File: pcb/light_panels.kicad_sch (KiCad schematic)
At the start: 31 parts, among them Y1 32.768kHz

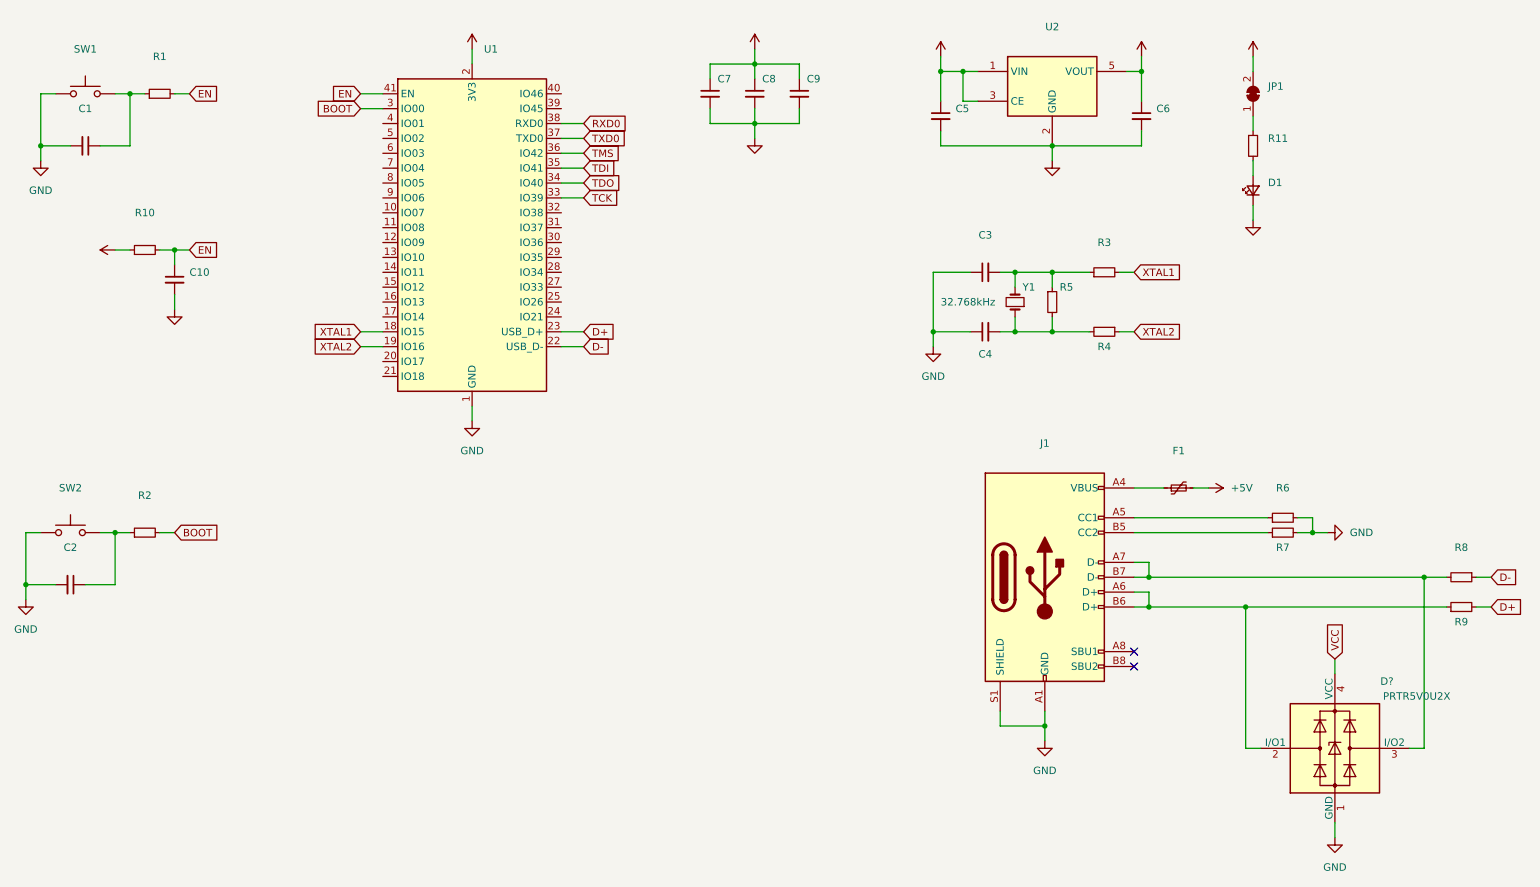
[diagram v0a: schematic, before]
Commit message: Added ferrite beads FB1 and 2
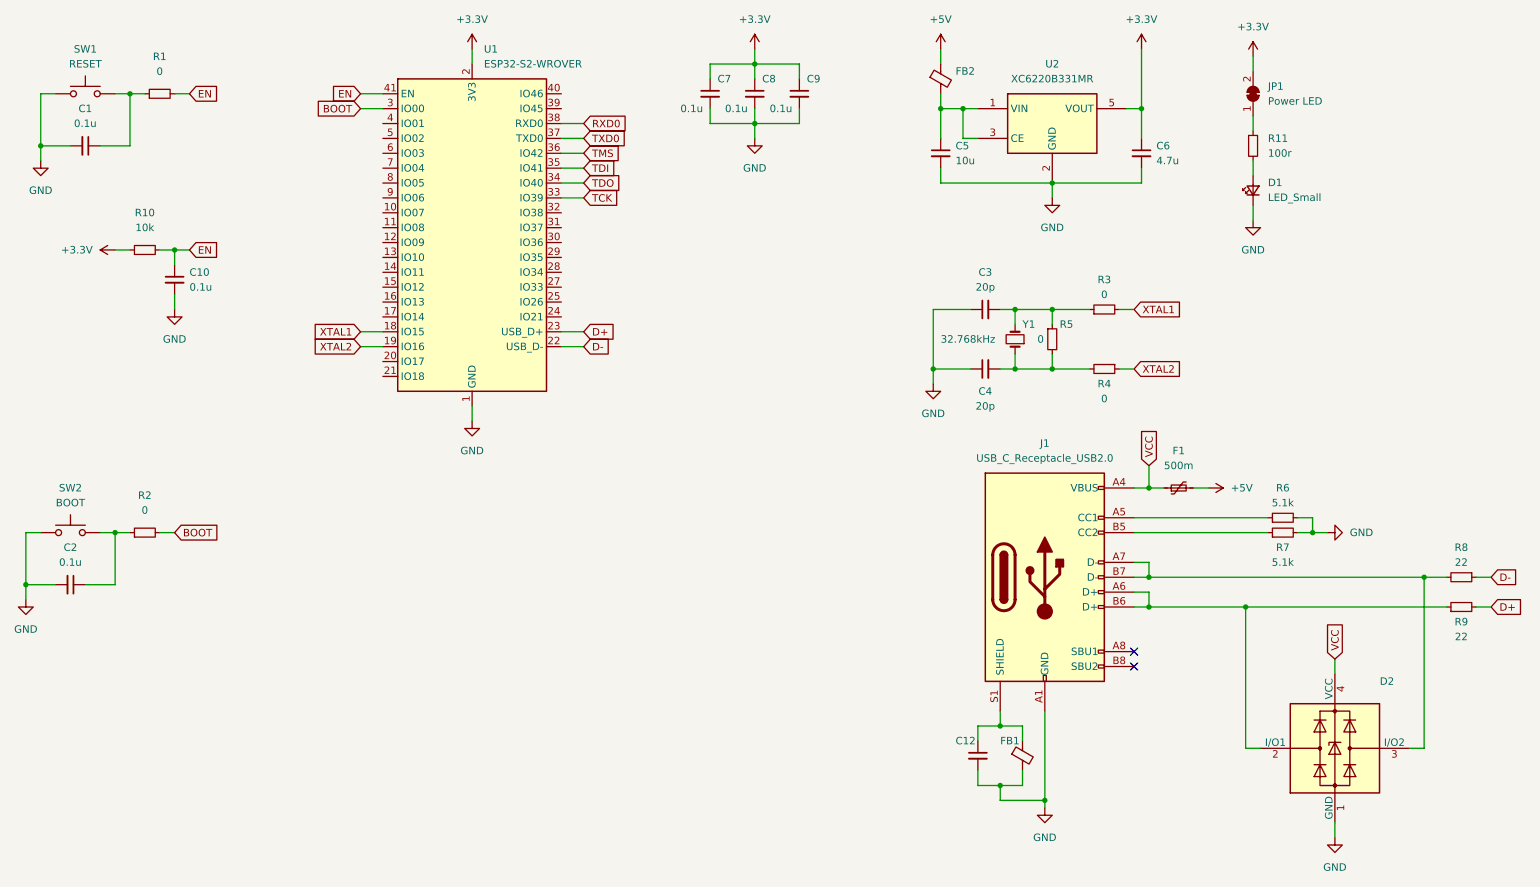
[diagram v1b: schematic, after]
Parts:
- added C12: (no value), symbol Device:C_Small
- added FB1, FB2: (no value), symbol Device:FerriteBead_Small
- C1, C10, C2, C7, C8, C9: value (none) -> 0.1u; footprint (none) -> Capacitor_SMD:C_0805_2012Metric
- C3, C4: value (none) -> 20p; footprint (none) -> Capacitor_SMD:C_0805_2012Metric
- C5: value (none) -> 10u; footprint (none) -> Capacitor_SMD:C_0805_2012Metric
- C6: value (none) -> 4.7u
- D1: value (none) -> LED_Small; footprint (none) -> LED_SMD:LED_0805_2012Metric
- D2: renamed from D?; value PRTR5V0U2X -> (none); footprint Package_TO_SOT_SMD:SOT-143 -> (none)
- F1: value (none) -> 500m
- J1: value (none) -> USB_C_Receptacle_USB2.0
- JP1: value (none) -> Power LED; footprint (none) -> Jumper:SolderJumper-2_P1.3mm_Bridged_RoundedPad1.0x1.5mm
- R1, R2, R3, R4, R5: value (none) -> 0; footprint (none) -> Resistor_SMD:R_0805_2012Metric
- R10: value (none) -> 10k; footprint (none) -> Resistor_SMD:R_0805_2012Metric
- R11: value (none) -> 100r; footprint (none) -> Resistor_SMD:R_0805_2012Metric
- R6, R7: value (none) -> 5.1k; footprint (none) -> Resistor_SMD:R_0805_2012Metric
- R8, R9: value (none) -> 22; footprint (none) -> Resistor_SMD:R_0805_2012Metric
- SW1: value (none) -> RESET
- SW2: value (none) -> BOOT
- U1: value (none) -> ESP32-S2-WROVER; footprint (none) -> RF_Module:ESP32-S2-WROVER
- U2: value (none) -> XC6220B331MR; footprint (none) -> Package_TO_SOT_SMD:SOT-23-5
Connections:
- net +5V: now also FB2.1; no longer C5.1, U2.1 (VIN), U2.3 (CE)
- net GND: now also C12.2, FB1.2; no longer J1.S1 (SHIELD)
- net VCC: now also F1.1, J1.A4 (VBUS), J1.A9 (VBUS), J1.B4 (VBUS), J1.B9 (VBUS)
- new net: C5.1, FB2.2, U2.1 (VIN), U2.3 (CE)
- new net: C12.1, FB1.1, J1.S1 (SHIELD)
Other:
- moved on the sheet: C3, C4, C5, C6, R3, R4, R5, U2, Y1
